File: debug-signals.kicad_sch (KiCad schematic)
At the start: 77 parts, among them U10 TCA9534PWR, U11 TCA9534PWR, U12 Si7021, U13 TCA9534PWR, U14 TCA9534PWR

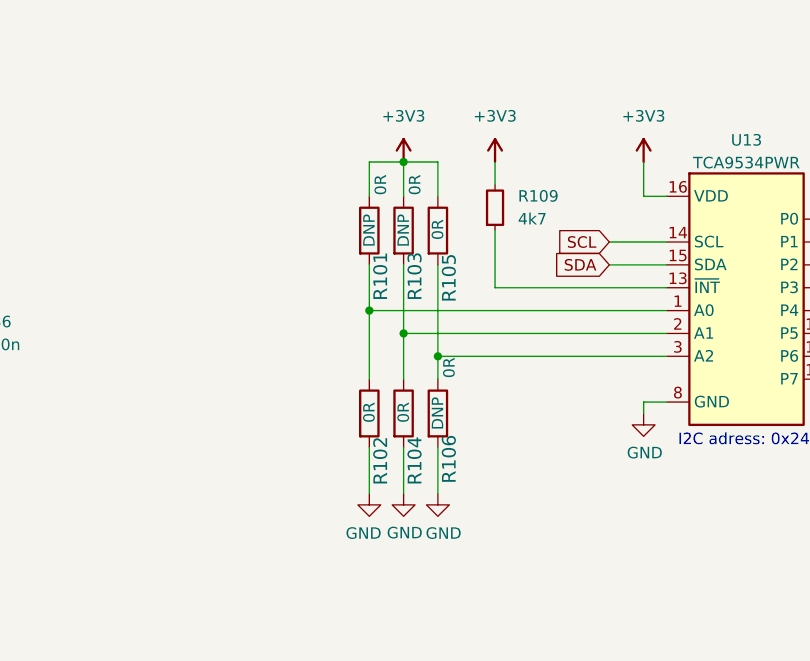
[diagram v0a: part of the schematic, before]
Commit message: Standarize missing components
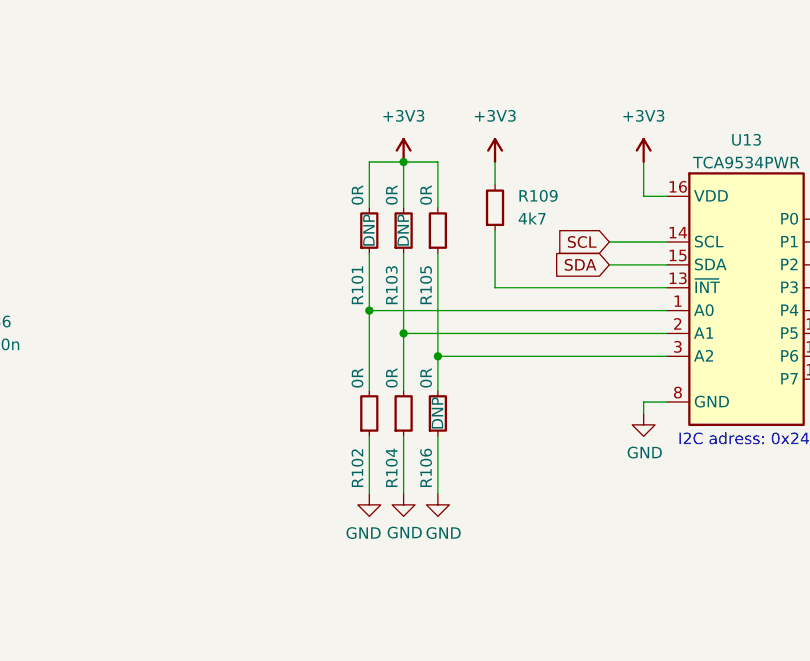
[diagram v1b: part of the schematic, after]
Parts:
- R101, R102, R103, R104, R105, R106: Author (none) -> Antmicro; Current (none) -> 1A; License (none) -> Apache-2.0; Manufacturer PANASONIC -> Panasonic
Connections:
- net +3V3: now also R101.2, R103.2, R105.2; no longer R101.1, R103.1, R105.1
- net GND: now also R102.1, R104.1, R106.1; no longer R102.2, R104.2, R106.2
- new net: R105.1, R106.2, U13.3 (A2)
- new net: R101.1, R102.2, U13.1 (A0)
- new net: R103.1, R104.2, U13.2 (A1)

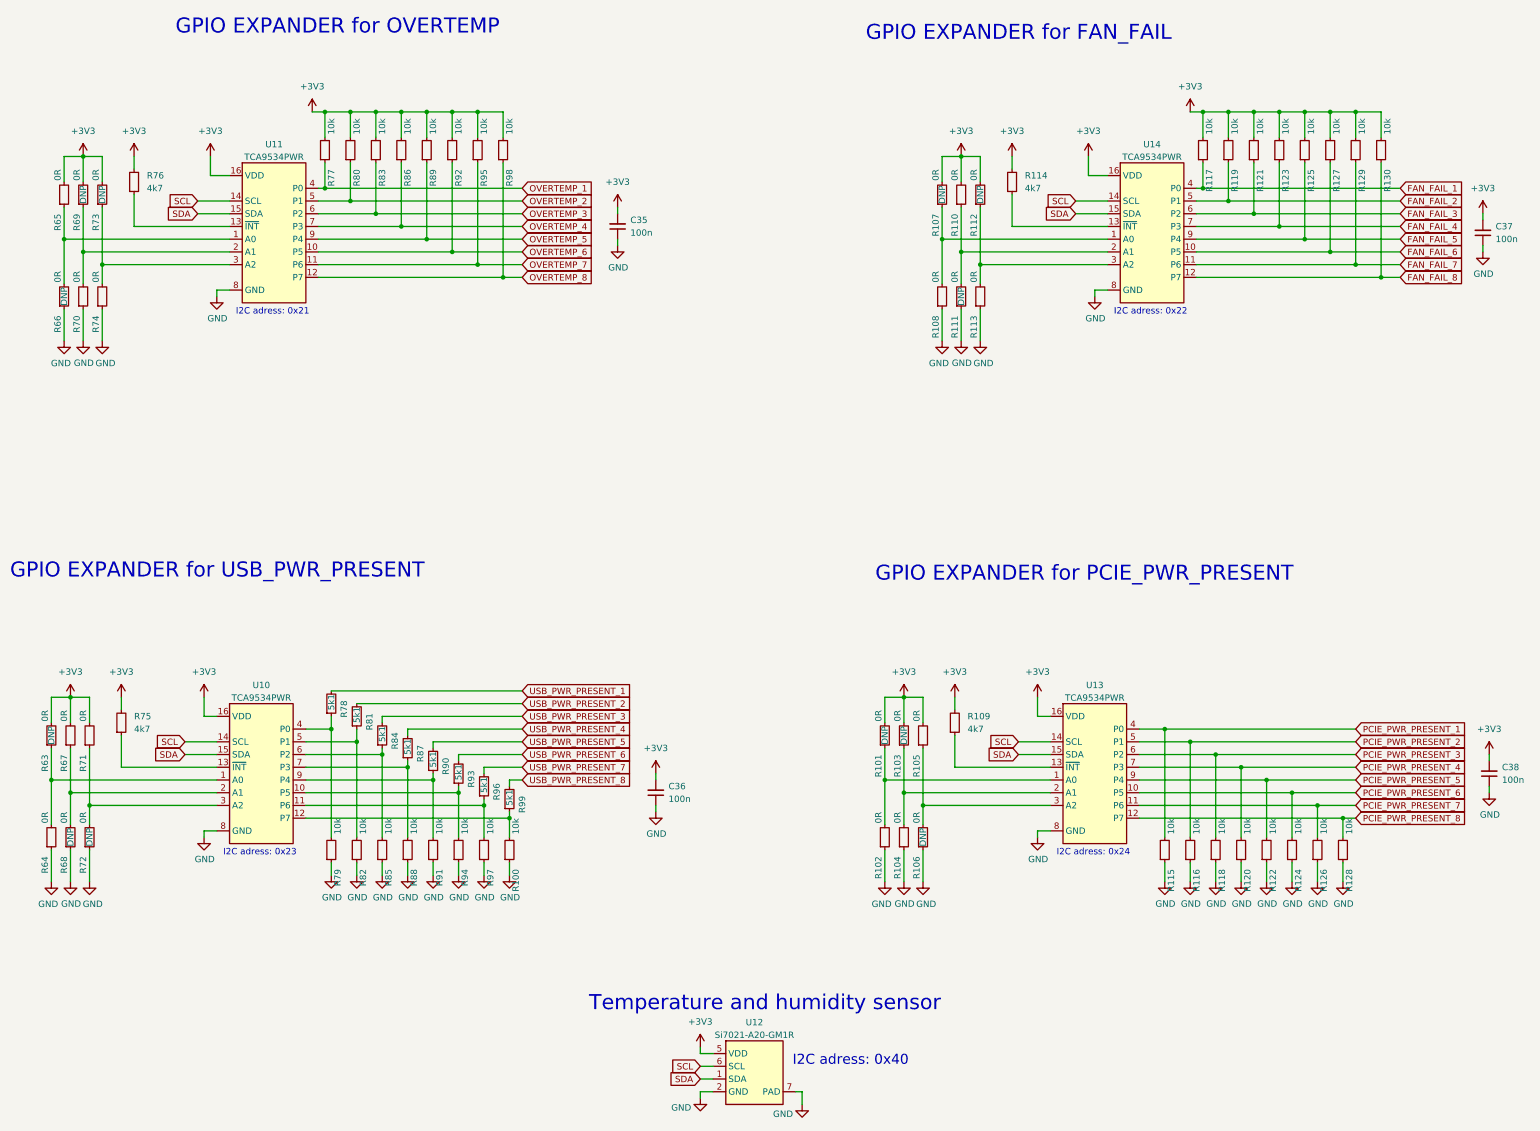
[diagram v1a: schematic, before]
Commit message: Add mux for temp signals
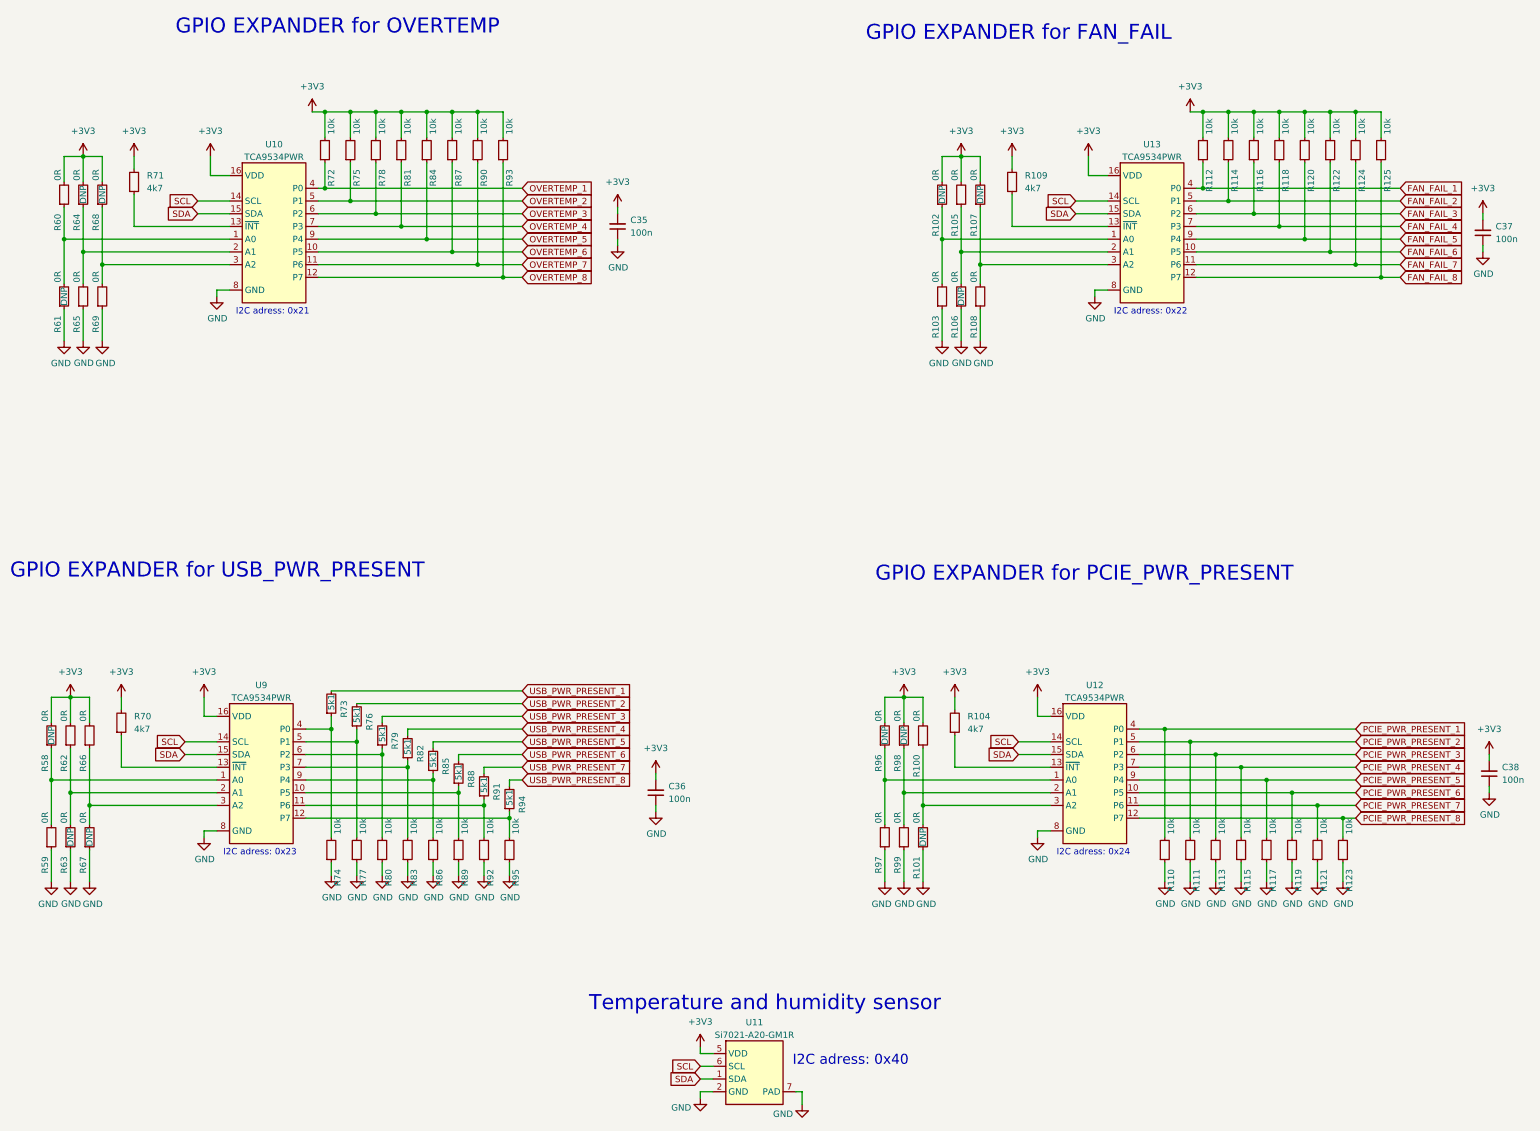
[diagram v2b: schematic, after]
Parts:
- renumbered R105 to R100, R106 to R101, R107 to R102, R108 to R103, R109 to R104, R110 to R105, R111 to R106, R112 to R107, R113 to R108, R114 to R109, R115 to R110, R116 to R111, R117 to R112, R118 to R113, R119 to R114, R120 to R115, R121 to R116, R122 to R117, R123 to R118, R124 to R119, R125 to R120, R126 to R121, R127 to R122, R128 to R123, R129 to R124, R130 to R125, R63 to R58, R64 to R59, R65 to R60, R66 to R61, R67 to R62, R68 to R63, R69 to R64, R70 to R65, R71 to R66, R72 to R67, R73 to R68, R74 to R69, R75 to R70, R76 to R71, R77 to R72, R78 to R73, R79 to R74, R80 to R75, R81 to R76, R82 to R77, R83 to R78, R84 to R79, R85 to R80, R86 to R81, R87 to R82, R88 to R83, R89 to R84, R90 to R85, R91 to R86, R92 to R87, R93 to R88, R94 to R89, R95 to R90, R96 to R91, R97 to R92, R98 to R93, R99 to R94, R100 to R95, R101 to R96, R102 to R97, R103 to R98, R104 to R99, U11 to U10, U12 to U11, U13 to U12, U14 to U13, U10 to U9

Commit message: Reannotate
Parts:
- renumbered C35 to C36, C36 to C37, C37 to C38, C38 to C39

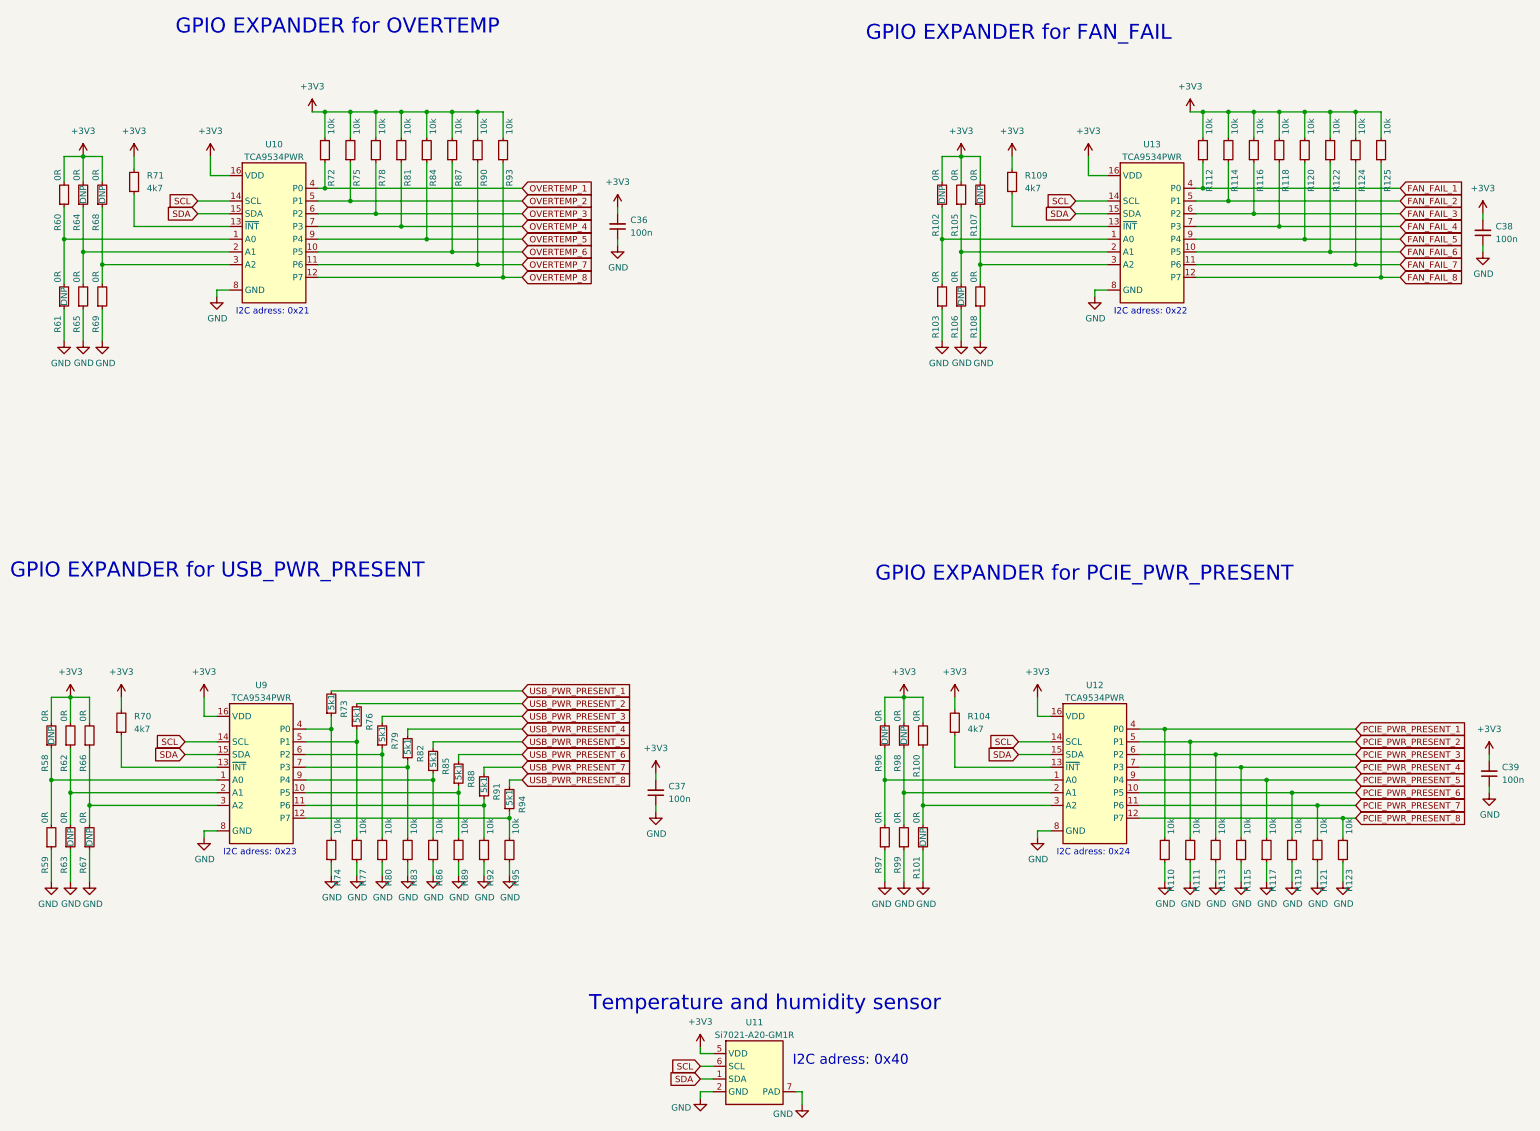
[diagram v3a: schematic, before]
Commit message: Standarize all components and enumerate
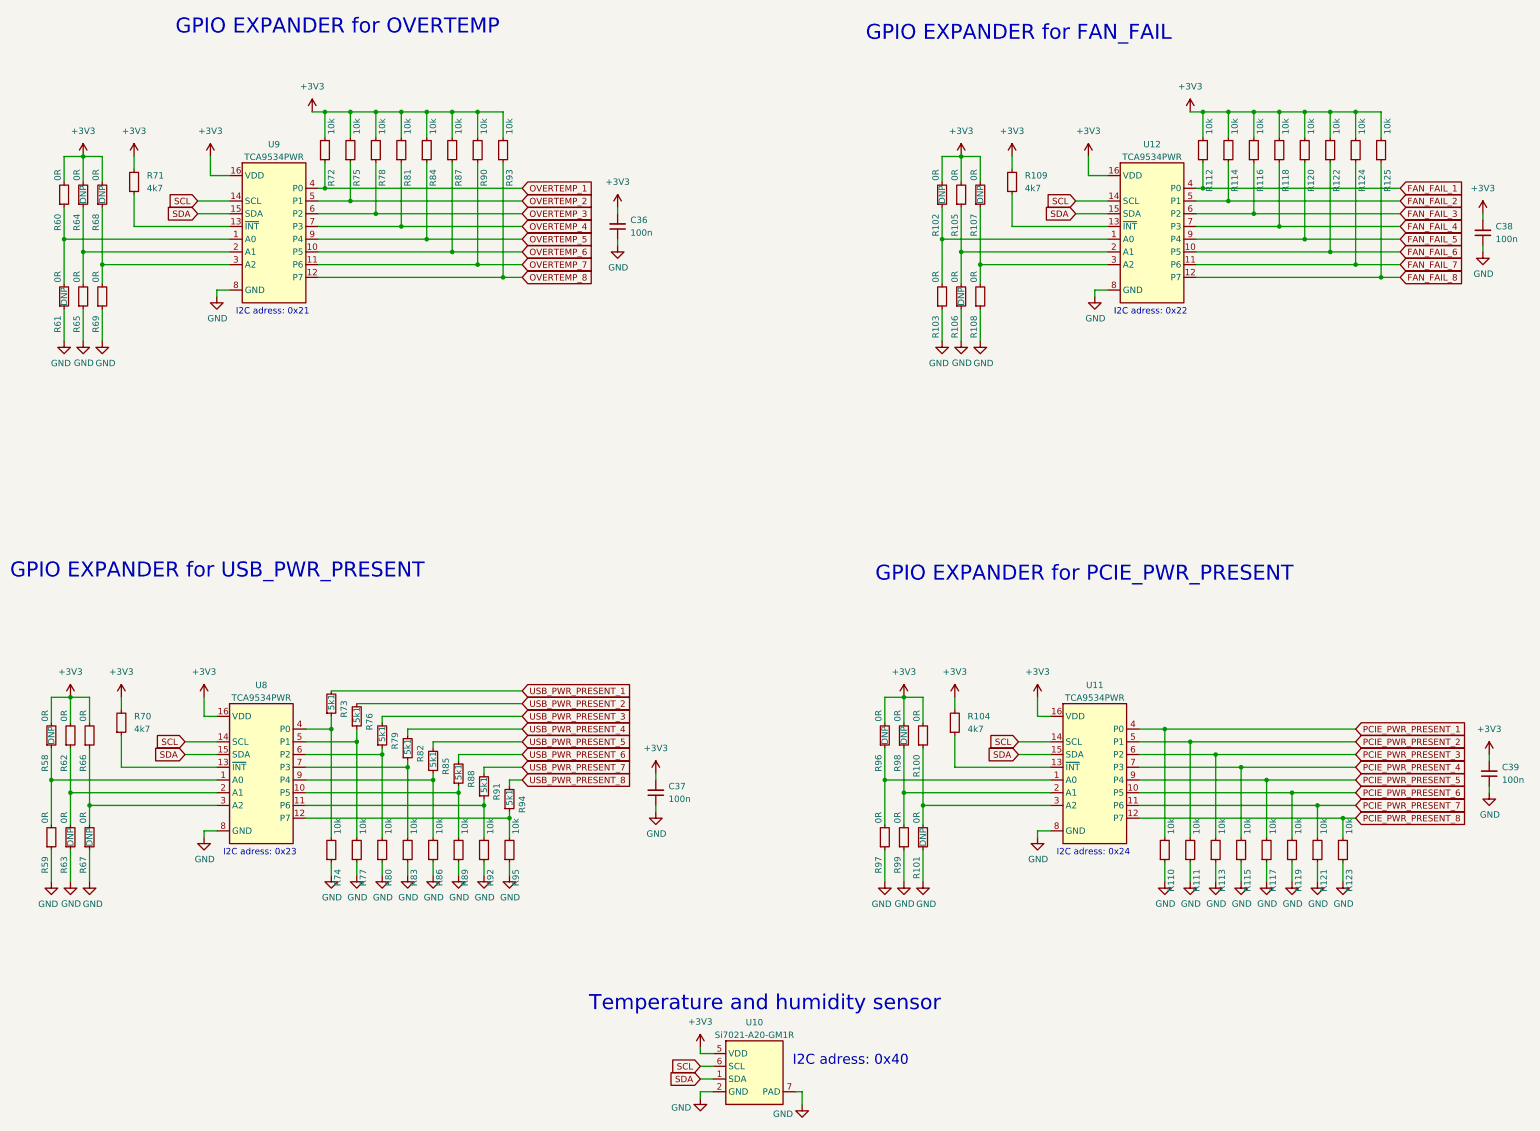
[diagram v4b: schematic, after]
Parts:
- renumbered U11 to U10, U12 to U11, U13 to U12, U9 to U8, U10 to U9

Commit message: Reannotate
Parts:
- renumbered C36 to C39, C37 to C40, C38 to C41, C39 to C42, R92 to R100, R93 to R101, R94 to R102, R95 to R103, R96 to R104, R97 to R105, R98 to R106, R99 to R107, R100 to R108, R101 to R109, R102 to R110, R103 to R111, R104 to R112, R105 to R113, R106 to R114, R107 to R115, R108 to R116, R109 to R117, R110 to R118, R111 to R119, R112 to R120, R113 to R121, R114 to R122, R115 to R123, R116 to R124, R117 to R125, R118 to R126, R119 to R127, R120 to R128, R121 to R129, R122 to R130, R123 to R131, R124 to R132, R125 to R133, R58 to R66, R59 to R67, R60 to R68, R61 to R69, R62 to R70, R63 to R71, R64 to R72, R65 to R73, R66 to R74, R67 to R75, R68 to R76, R69 to R77, R70 to R78, R71 to R79, R72 to R80, R73 to R81, R74 to R82, R75 to R83, R76 to R84, R77 to R85, R78 to R86, R79 to R87, R80 to R88, R81 to R89, R82 to R90, R83 to R91, R84 to R92, R85 to R93, R86 to R94, R87 to R95, R88 to R96, R89 to R97, R90 to R98, R91 to R99, U8 to U11, U9 to U12, U10 to U13, U11 to U14, U12 to U15

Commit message: Additional cleanup
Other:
- title: (none) -> GPU Cluster Backplane
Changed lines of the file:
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@@
 (kicad_sch (version 20211123) (generator eeschema)
   (paper "A3")
+  (title_block
+    (title "GPU Cluster Backplane")
+    (date "2023-10-18")
+    (rev "1.0.0")
+    (comment 1 "www.antmicro.com")
+    (comment 2 "Antmicro Ltd.")
+  )
   (junction (at 128.27 71.12) (diameter 0) (color 0 0 0 0)
   )
